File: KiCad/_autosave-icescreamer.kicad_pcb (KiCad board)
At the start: 2 copper layers, 60 x 20 mm, 84 parts, among them J1 Audio-Jack-3_3Switches, J2 Audio-Jack-3_3Switches, Q1 2SC1815, Q2 2SC1815, Q20 2SC1815, Q21 2SC1815, Q22 2SC1815, Q23 Q_NJFET_SGD, Q24 Q_NJFET_SGD, SW1 SW_TPDT, SW20 SW_Push, U1 NE5532

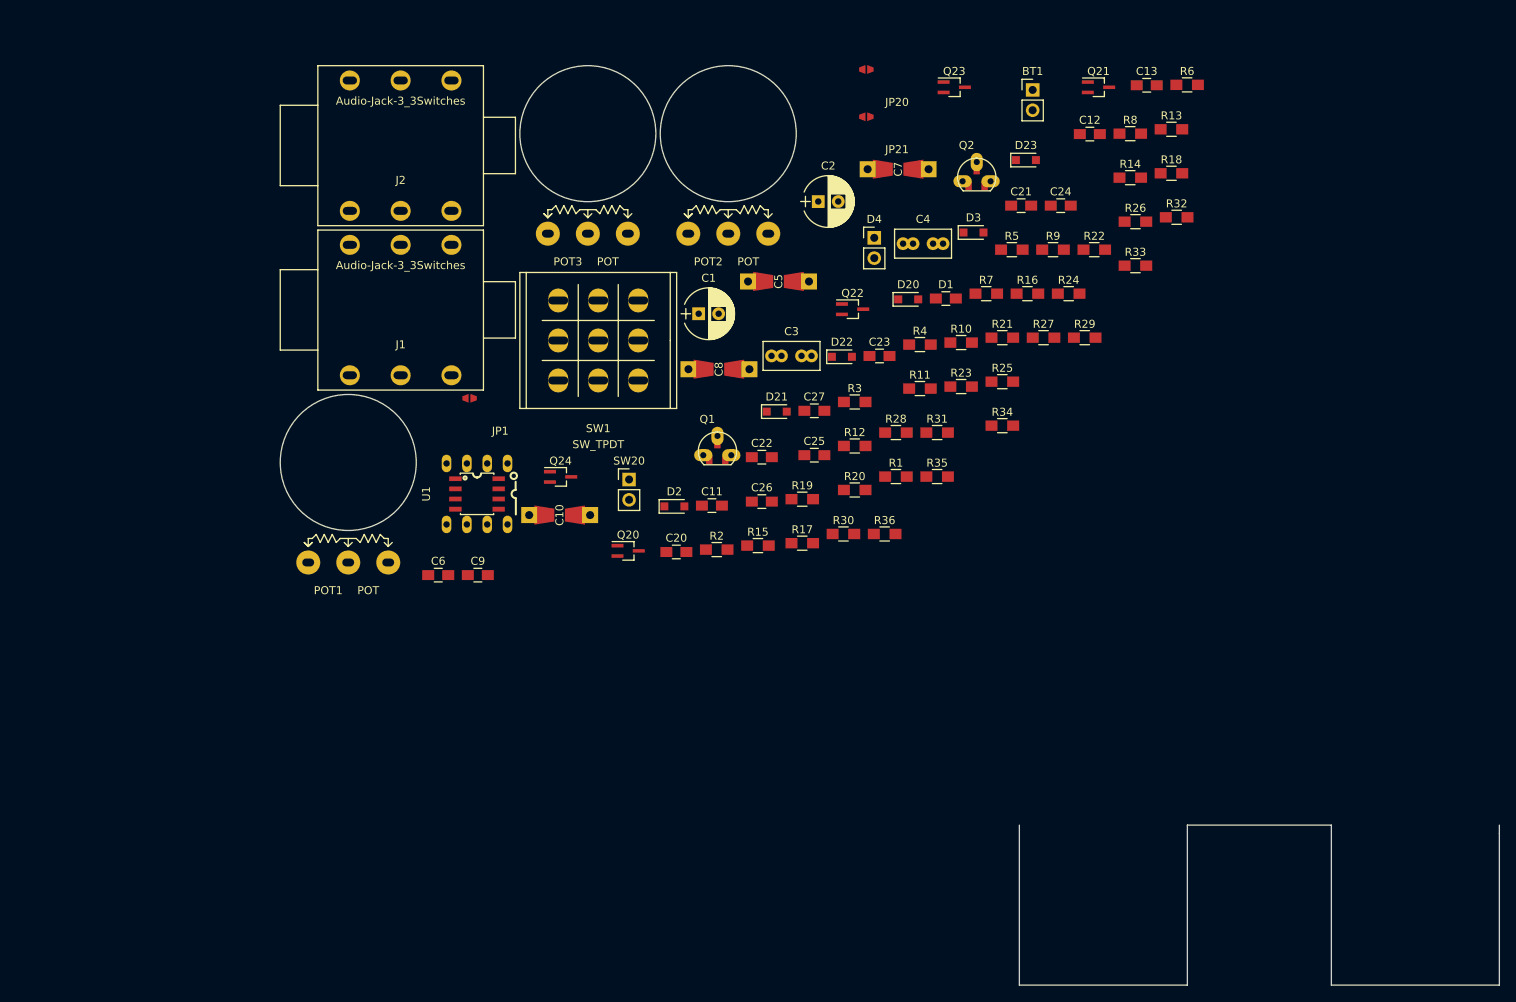
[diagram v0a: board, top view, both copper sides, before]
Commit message: Añadidos archivos de huellas
DIP8+SOIC8 importado de Drawdio
3PDT tomado de def-footprints
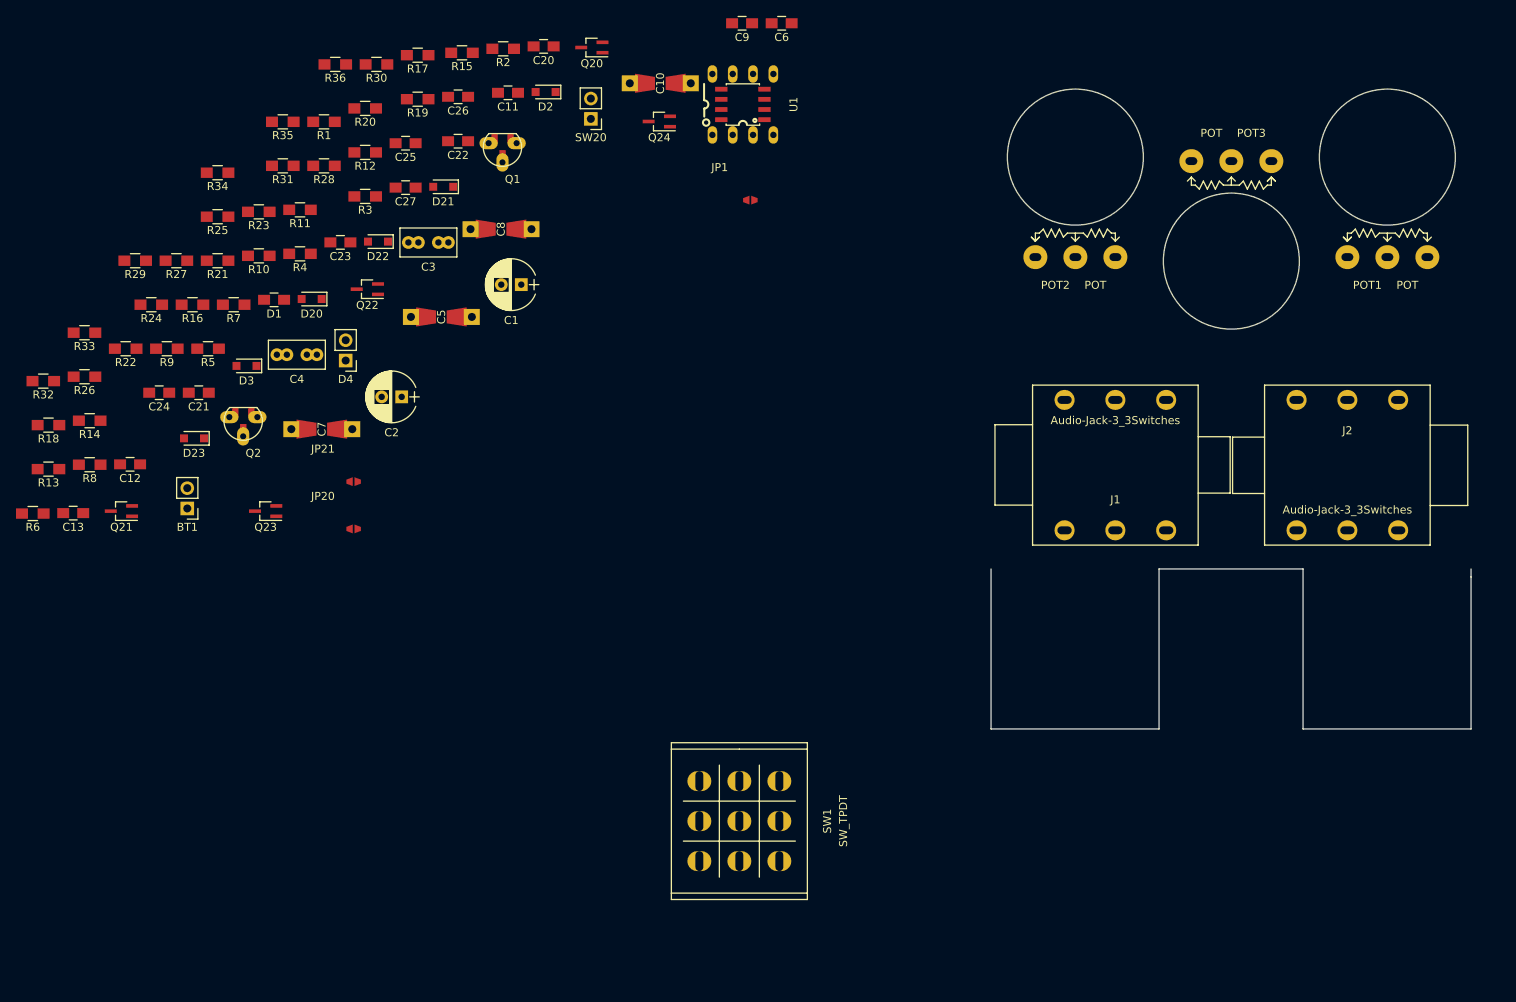
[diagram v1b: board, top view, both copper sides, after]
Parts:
- moved R6 153.9 mm to (63.7, 113.1), turned to 180 degrees
- moved R13 146.7 mm to (65.6, 107.5), turned to 180 degrees
- moved C13 144.5 mm to (68.7, 113.0), turned to 180 degrees
- moved R18 143.9 mm to (65.6, 102.0), turned to 180 degrees
- moved R32 143.1 mm to (65.0, 96.5), turned to 180 degrees
- moved R8 136.5 mm to (70.8, 107.0), turned to 180 degrees
- moved POT1 135.4 mm to (233.0, 68.5)
- moved R14 133.6 mm to (70.8, 101.5), turned to 180 degrees
- moved Q21 133.1 mm to (74.8, 112.8), turned to 180 degrees
- moved R26 132.8 mm to (70.1, 96.0), turned to 180 degrees
- moved R33 131.6 mm to (70.1, 90.5), turned to 180 degrees
- moved C12 126.9 mm to (75.8, 106.9), turned to 180 degrees
- moved J2 124.9 mm to (228.0, 107.0), turned to 180 degrees
- moved R22 121.7 mm to (75.3, 92.5), turned to 180 degrees
- moved R29 119.1 mm to (76.5, 81.5), turned to 180 degrees
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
